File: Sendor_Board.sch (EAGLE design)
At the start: 54 parts, among them Q1 8.000Mhz, T1 IRLM6402TRPBF, U1 PIC32MX795F512H-80I/PT, U2 SHT25, U3 MPL115A2, U4 MRF24J40MA, U5 TC1262-3.3VDB, U6 VTX-214-003-105, X1 MINI-USB-SHIELD-UX60A-MB-5ST, X3 MKDSN1,5/4-5,08

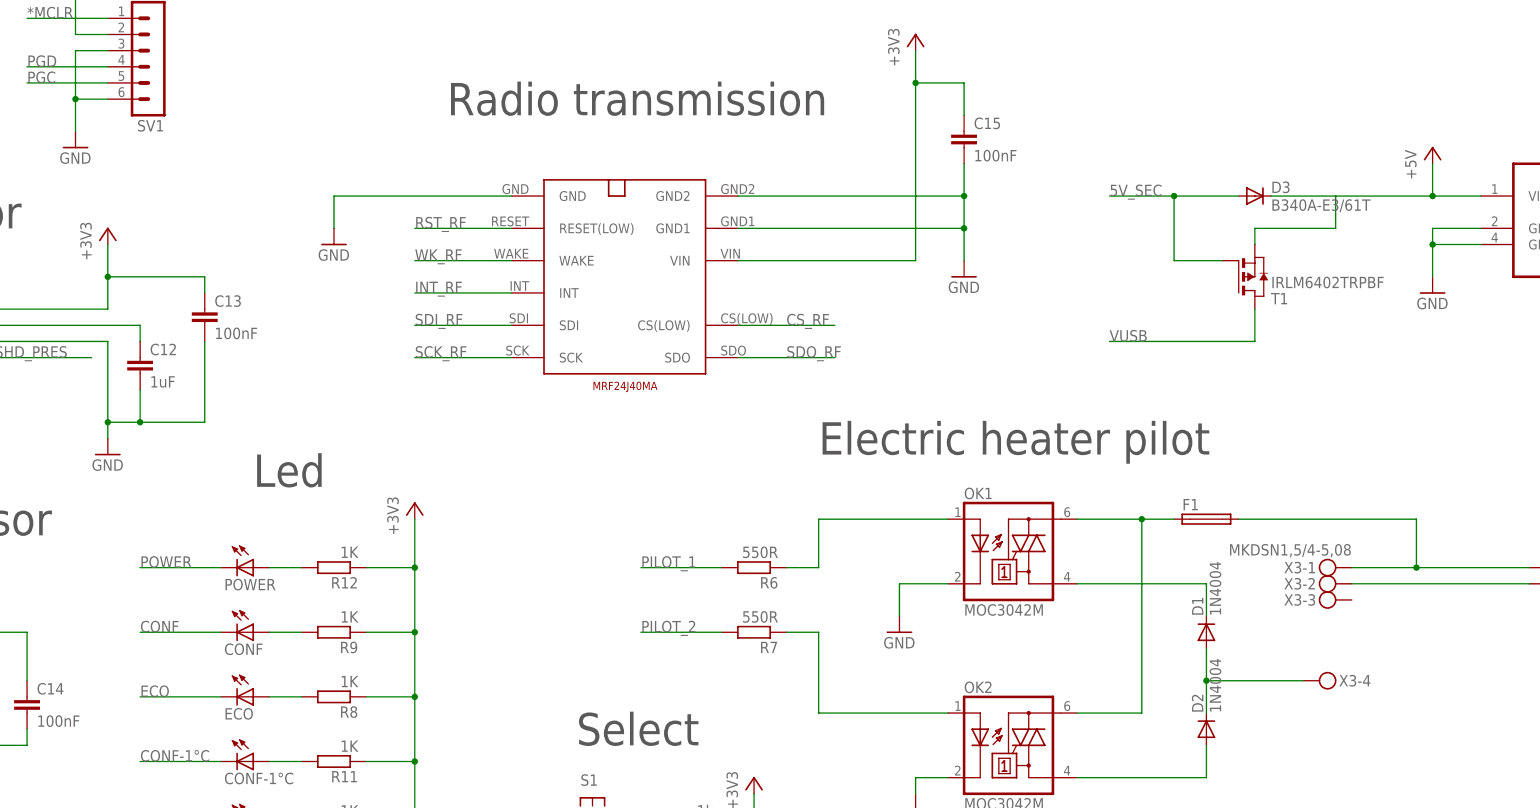
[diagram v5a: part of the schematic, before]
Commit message: Change PHOENIX connector type
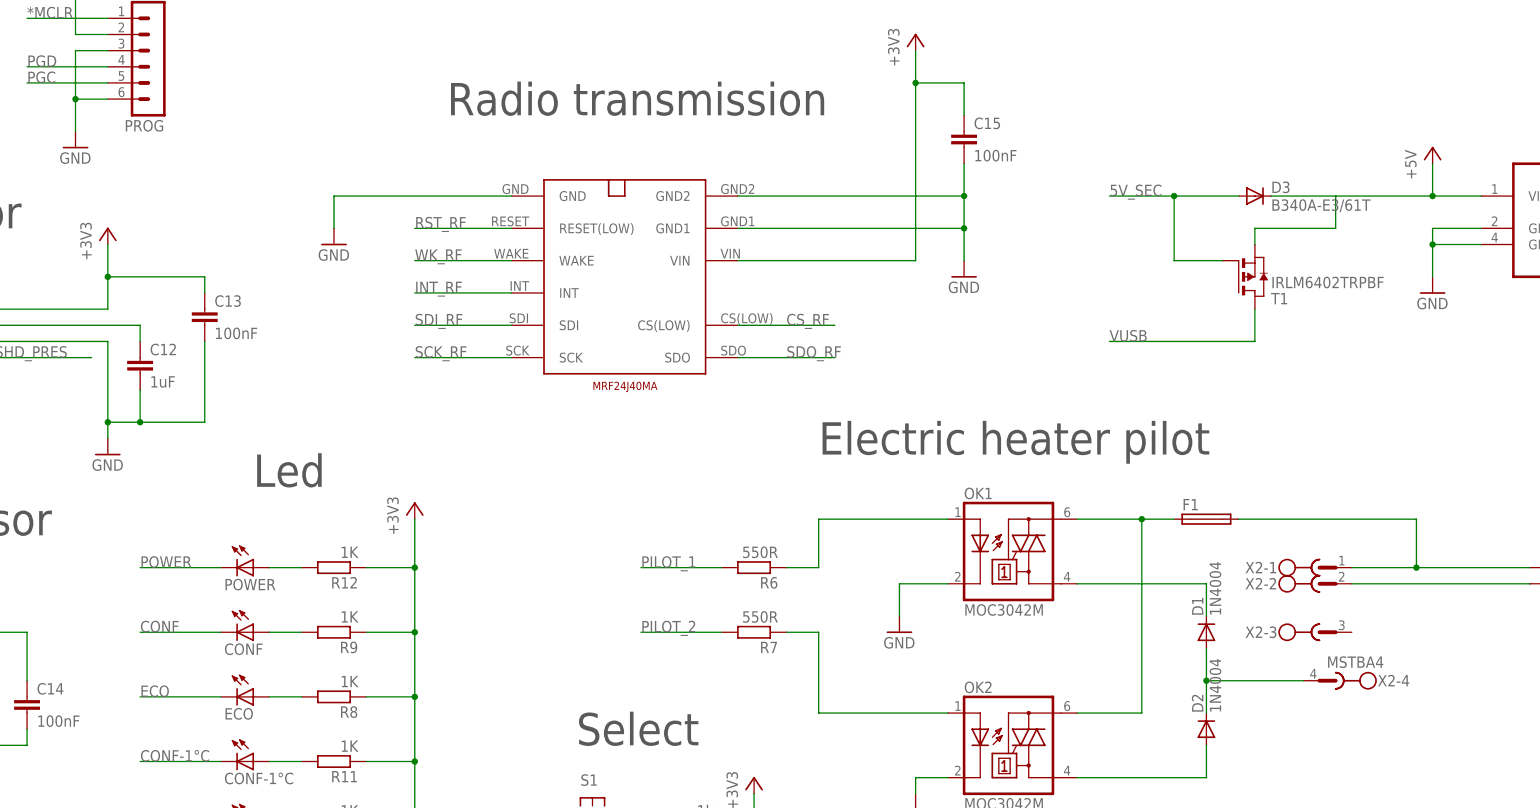
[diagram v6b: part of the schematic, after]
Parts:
- removed X3: MKDSN1,5/4-5,08, con-phoenix-508:MKDSN1,5/4-5,08
- added X2: MSTBA4, con-phoenix-508:MSTBA4
- renumbered SV1 to PROG
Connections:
- net N$11: now also X2-1.1; no longer X3-1.KL
- net N$15: now also X2-4.1; no longer X3-4.KL
- net N$17: now also X2-2.1; no longer X3-2.KL
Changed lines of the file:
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@@
 </part>
 <part name="GND16" library="supply1" deviceset="GND" device=""/>
-<part name="X3" library="con-phoenix-508" deviceset="MKDSN1,5/4-5,08" device=""/>
 <part name="U6" library="pfo" deviceset="VTX-214-003-105" device=""/>
 <part name="GND17" library="supply1" deviceset="GND" device=""/>
 <part name="T1" library="zetex" deviceset="PMOSSOT23" device="" value="IRLM6402TRPBF"/>
 <part name="D3" library="diode" deviceset="DIODE-" device="DO214AC" value="B340A-E3/61T"/>
-<part name="SV1" library="con-lstb" deviceset="MA06-1" device=""/>
+<part name="PROG" library="con-lstb" deviceset="MA06-1" device=""/>
 <part name="GND18" library="supply1" deviceset="GND" device=""/>
 <part name="+3V7" library="supply1" deviceset="+3V3" device=""/>
@@
 <part name="R13" library="resistor" deviceset="R-EU_" device="R1206" value="1k"/>
 <part name="+3V9" library="supply1" deviceset="+3V3" device=""/>
+<part name="X2" library="con-phoenix-508" deviceset="MSTBA4" device=""/>
 </parts>
 <sheets>
@@
 </instance>
 <instance part="GND16" gate="1" x="238.76" y="-53.34"/>
-<instance part="X3" gate="-1" x="162.56" y="-91.44" rot="R180"/>
-<instance part="X3" gate="-2" x="162.56" y="-93.98" rot="R180"/>
-<instance part="X3" gate="-3" x="162.56" y="-96.52" rot="R180"/>
-<instance part="X3" gate="-4" x="160.02" y="-109.22"/>
 <instance part="U6" gate="G$1" x="208.28" y="-93.98"/>
 <instance part="GND17" gate="1" x="231.14" y="-106.68"/>
 <instance part="T1" gate="A" x="149.86" y="-45.72" rot="MR180"/>
 <instance part="D3" gate="G$1" x="149.86" y="-33.02"/>
-<instance part="SV1" gate="1" x="-22.86" y="-12.7" rot="R180"/>
+<instance part="PROG" gate="1" x="-22.86" y="-12.7" rot="R180"/>
 <instance part="GND18" gate="1" x="-35.56" y="-25.4"/>
 <instance part="+3V7" gate="G$1" x="-35.56" y="5.08"/>
@@
 <instance part="R13" gate="G$1" x="60.96" y="-132.08" rot="R180"/>
 <instance part="+3V9" gate="G$1" x="71.12" y="-124.46"/>
+<instance part="X2" gate="-1" x="160.02" y="-91.44"/>
+<instance part="X2" gate="-2" x="160.02" y="-93.98"/>
+<instance part="X2" gate="-3" x="160.02" y="-101.6"/>
+<instance part="X2" gate="-4" x="162.56" y="-109.22" rot="R180"/>
 </instances>
 <busses>
@@
 </segment>
 <segment>
-<pinref part="SV1" gate="1" pin="3"/>
+<pinref part="PROG" gate="1" pin="3"/>
 <wire x1="-30.48" y1="-10.16" x2="-35.56" y2="-10.16" width="0.1524" layer="91"/>
-<pinref part="SV1" gate="1" pin="6"/>
+<pinref part="PROG" gate="1" pin="6"/>
 <wire x1="-30.48" y1="-17.78" x2="-35.56" y2="-17.78" width="0.1524" layer="91"/>
 <wire x1="-35.56" y1="-10.16" x2="-35.56" y2="-17.78" width="0.1524" layer="91"/>
@@
 </segment>
 <segment>
-<pinref part="SV1" gate="1" pin="2"/>
+<pinref part="PROG" gate="1" pin="2"/>
 <wire x1="-30.48" y1="-7.62" x2="-35.56" y2="-7.62" width="0.1524" layer="91"/>
 <wire x1="-35.56" y1="-7.62" x2="-35.56" y2="2.54" width="0.1524" layer="91"/>
@@
 </segment>
 <segment>
-<pinref part="SV1" gate="1" pin="1"/>
+<pinref part="PROG" gate="1" pin="1"/>
 <wire x1="-30.48" y1="-5.08" x2="-43.18" y2="-5.08" width="0.1524" layer="91"/>
 <label x="-43.18" y="-5.08" size="1.778" layer="95"/>
@@
 <segment>
 <pinref part="F1" gate="1" pin="2"/>
-<pinref part="X3" gate="-1" pin="KL"/>
 <wire x1="165.1" y1="-91.44" x2="175.26" y2="-91.44" width="0.1524" layer="91"/>
 <wire x1="175.26" y1="-91.44" x2="175.26" y2="-83.82" width="0.1524" layer="91"/>
@@
 <wire x1="175.26" y1="-91.44" x2="193.04" y2="-91.44" width="0.1524" layer="91"/>
 <pinref part="U6" gate="G$1" pin="AC1"/>
+<pinref part="X2" gate="-1" pin="1"/>
 </segment>
 </net>
@@
 <wire x1="142.24" y1="-109.22" x2="157.48" y2="-109.22" width="0.1524" layer="91"/>
 <junction x="142.24" y="-109.22"/>
-<pinref part="X3" gate="-4" pin="KL"/>
+<pinref part="X2" gate="-4" pin="1"/>
 </segment>
 </net>
 <net name="N$17" class="0">
 <segment>
-<pinref part="X3" gate="-2" pin="KL"/>
 <wire x1="165.1" y1="-93.98" x2="193.04" y2="-93.98" width="0.1524" layer="91"/>
 <pinref part="U6" gate="G$1" pin="AC2"/>
+<pinref part="X2" gate="-2" pin="1"/>
 </segment>
 </net>
@@
 <net name="PGD" class="0">
 <segment>
-<pinref part="SV1" gate="1" pin="4"/>
+<pinref part="PROG" gate="1" pin="4"/>
 <wire x1="-30.48" y1="-12.7" x2="-43.18" y2="-12.7" width="0.1524" layer="91"/>
 <label x="-43.18" y="-12.7" size="1.778" layer="95"/>
@@
 <net name="PGC" class="0">
 <segment>
-<pinref part="SV1" gate="1" pin="5"/>
+<pinref part="PROG" gate="1" pin="5"/>
 <wire x1="-30.48" y1="-15.24" x2="-43.18" y2="-15.24" width="0.1524" layer="91"/>
 <label x="-43.18" y="-15.24" size="1.778" layer="95"/>
